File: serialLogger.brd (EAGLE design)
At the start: 63.5 x 50.8 mm, 36 parts, among them J1 Ext Pwr, U1 MCP1702, U2 MCP1700, U3 ATmega328P-AU, U4 74HC4050PW, X1 MICROSD, Y1 16MHz

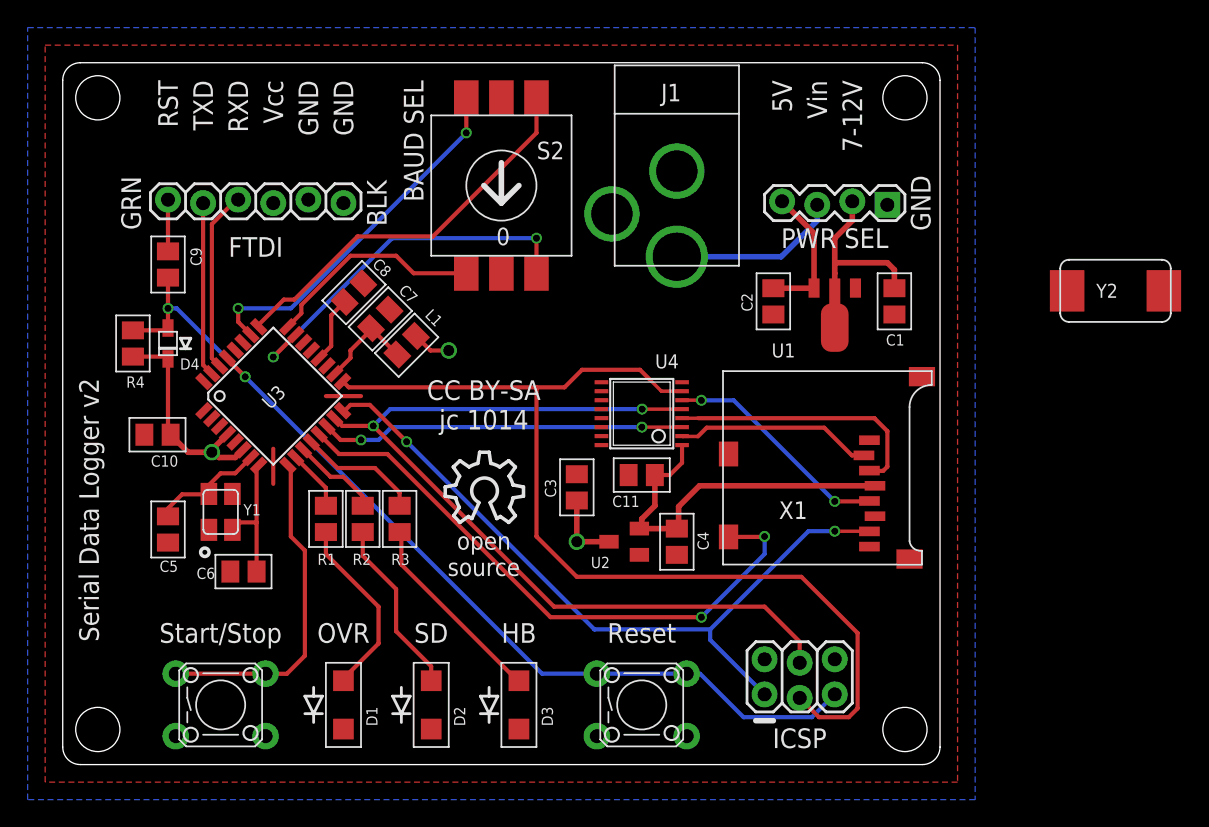
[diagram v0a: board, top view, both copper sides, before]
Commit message: Change to Abracon xtal, refine board, add BOM spreadsheet.
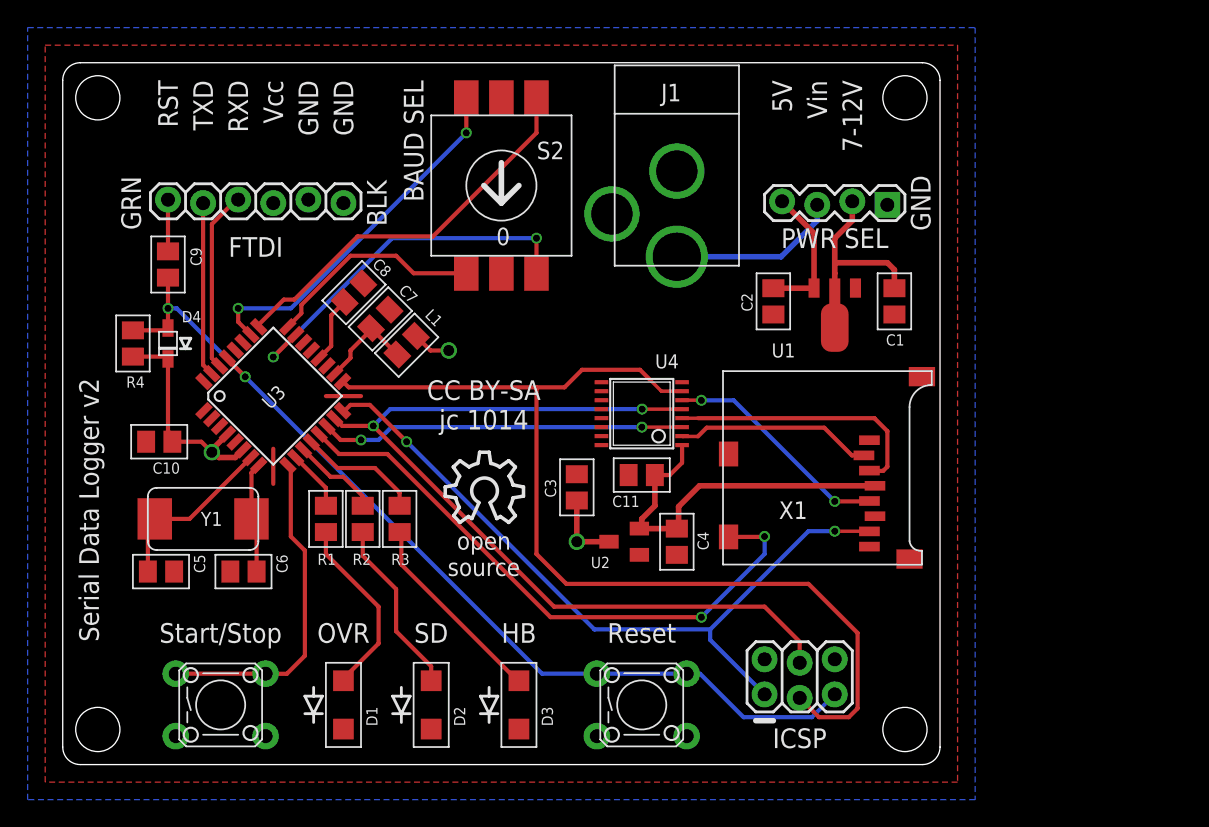
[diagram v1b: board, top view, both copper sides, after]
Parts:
- removed Y2: (no value), _jc:CRYSTAL-ABRACON-ABM2
- C5, C6: value 22pF -> 27pF
- Y1: device _jc:CRYSTAL-EPSON-TSX3225 -> _jc:CRYSTAL-ABRACON-ABM2
- moved C5 3.09 mm to (7.11, 14.0), turned to 0 degrees
- moved Y1 1.37 mm to (10.2, 17.8), turned to 180 degrees
- moved C10 0.52 mm to (6.99, 23.4)
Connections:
- net GND: no longer Y1.2, Y1.4
- net N$18: now also Y1.P$2; no longer Y1.1
- net N$19: now also Y1.P$1; no longer Y1.3
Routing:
- net N$18: track 8.47 -> 12.8 mm
- net N$19: track 9.72 -> 8.06 mm
- net SCK: track 73.3 -> 74.1 mm
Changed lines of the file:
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@@
 <layer number="22" name="bPlace" color="7" fill="1" visible="no" active="yes"/>
 <layer number="23" name="tOrigins" color="15" fill="1" visible="yes" active="yes"/>
-<layer number="24" name="bOrigins" color="15" fill="1" visible="yes" active="yes"/>
+<layer number="24" name="bOrigins" color="15" fill="1" visible="no" active="yes"/>
 <layer number="25" name="tNames" color="7" fill="1" visible="yes" active="yes"/>
 <layer number="26" name="bNames" color="7" fill="1" visible="yes" active="yes"/>
@@
 <layer number="49" name="Reference" color="7" fill="1" visible="yes" active="yes"/>
 <layer number="50" name="dxf" color="7" fill="1" visible="no" active="no"/>
-<layer number="51" name="tDocu" color="7" fill="1" visible="yes" active="yes"/>
+<layer number="51" name="tDocu" color="7" fill="1" visible="no" active="yes"/>
 <layer number="52" name="bDocu" color="7" fill="1" visible="yes" active="yes"/>
 <layer number="53" name="tGND_GNDA" color="7" fill="9" visible="no" active="no"/>
@@
 <attribute name="NAME" x="51.833" y="17.777" size="1.27" layer="25" ratio="16"/>
 </element>
-<element name="C10" library="_jc" package="M0805" value="100nF" x="6.858" y="23.876" smashed="yes" rot="R180">
-<attribute name="NAME" x="8.358" y="22.376003125" size="0.8128" layer="25" ratio="16" rot="R180"/>
-<attribute name="VALUE" x="8.357996875" y="26.376003125" size="0.8128" layer="27" ratio="16" rot="R180"/>
+<element name="C10" library="_jc" package="M0805" value="100nF" x="6.985" y="23.368" smashed="yes" rot="R180">
+<attribute name="NAME" x="8.485" y="21.868003125" size="0.8128" layer="25" ratio="16" rot="R180"/>
+<attribute name="VALUE" x="8.484996875" y="25.868003125" size="0.8128" layer="27" ratio="16" rot="R180"/>
 </element>
 <element name="C11" library="_jc" package="M0805" value="100nF" x="41.91" y="20.955" smashed="yes" rot="R180">
@@
 </element>
 <element name="D4" library="_jc" package="SOD-323F-A" value="1N4148" x="7.62" y="30.48" smashed="yes" rot="R270">
-<attribute name="NAME" x="8.487" y="28.586" size="0.8128" layer="25" font="vector" ratio="16"/>
+<attribute name="NAME" x="8.614" y="32.015" size="0.8128" layer="25" font="vector" ratio="16"/>
 <attribute name="VALUE" x="5.92" y="32.58" size="0.8128" layer="27" font="vector" ratio="16" rot="R270"/>
 </element>
@@
 <attribute name="VALUE" x="21.78910625" y="31.334571875" size="0.8128" layer="27" ratio="16" rot="R45"/>
 </element>
-<element name="C5" library="_jc" package="M0805" value="22pF" x="7.62" y="17.018" smashed="yes" rot="R270">
-<attribute name="NAME" x="7.009" y="13.946" size="0.8128" layer="25" ratio="16"/>
-<attribute name="VALUE" x="5.12" y="18.518" size="0.8128" layer="27" ratio="16" rot="R270"/>
-</element>
-<element name="C6" library="_jc" package="M0805" value="22pF" x="13.081" y="13.97" smashed="yes" rot="R180">
-<attribute name="NAME" x="11.025" y="14.248" size="0.8128" layer="25" ratio="16" rot="R180"/>
+<element name="C5" library="_jc" package="M0805" value="27pF" x="7.112" y="13.97" smashed="yes">
+<attribute name="NAME" x="10.311" y="13.867" size="0.8128" layer="25" ratio="16" rot="R90"/>
+<attribute name="VALUE" x="5.612" y="11.47" size="0.8128" layer="27" ratio="16"/>
+</element>
+<element name="C6" library="_jc" package="M0805" value="27pF" x="13.081" y="13.97" smashed="yes" rot="R180">
+<attribute name="NAME" x="16.28" y="13.867" size="0.8128" layer="25" ratio="16" rot="R90"/>
 <attribute name="VALUE" x="14.581" y="16.47" size="0.8128" layer="27" ratio="16" rot="R180"/>
 </element>
@@
 <attribute name="VALUE" x="24.184890625" y="33.181425" size="0.8128" layer="27" ratio="16" rot="R225"/>
 </element>
-<element name="Y1" library="_jc" package="CRYSTAL-EPSON-TSX3225" value="16MHz" x="11.43" y="18.288" smashed="yes" rot="R270">
-<attribute name="NAME" x="13.081" y="18.034" size="0.8128" layer="25" ratio="16"/>
-<attribute name="VALUE" x="8.89" y="19.558" size="0.8128" layer="27" ratio="16" rot="R270"/>
-</element>
 <element name="U2" library="_jc" package="SOT23" value="MCP1700" x="40.64" y="16.129" smashed="yes" rot="R90">
 <attribute name="NAME" x="38.227" y="14.224" size="0.8128" layer="25" ratio="16"/>
@@
 <element name="LOGO1" library="ohw-logo" package="OSHW_10X200_NOTEXT" value="OSHW_LOGO_10MILX0200-NT" x="27.686" y="17.526"/>
 <element name="LOGO2" library="ohw-logo" package="OSHW_10X200_NOTEXT" value="OSHW_LOGO_10MILX0200-NT" x="32.004" y="37.846" rot="MR0"/>
-<element name="Y2" library="_jc" package="CRYSTAL-ABRACON-ABM2" value="" x="76.2" y="34.29"/>
+<element name="Y1" library="_jc" package="CRYSTAL-ABRACON-ABM2" value="16MHz" x="10.16" y="17.78" rot="R180"/>
 </elements>
 <signals>
@@
 <contactref element="U3" pad="3"/>
 <contactref element="U3" pad="5"/>
-<contactref element="Y1" pad="2"/>
-<contactref element="Y1" pad="4"/>
 <contactref element="C7" pad="2"/>
 <contactref element="C8" pad="2"/>
@@
 <wire x1="5.08" y1="29.53" x2="7.4524" y2="29.53" width="0.3048" layer="1"/>
 <wire x1="7.4524" y1="29.53" x2="7.62" y2="29.3624" width="0.3048" layer="1"/>
-<wire x1="7.808" y1="23.876" x2="9.078" y2="22.606" width="0.4064" layer="1"/>
-<wire x1="9.078" y1="22.606" x2="10.795" y2="22.606" width="0.4064" layer="1"/>
-<wire x1="7.808" y1="23.876" x2="7.62" y2="24.064" width="0.3048" layer="1"/>
-<wire x1="7.62" y1="24.064" x2="7.62" y2="29.3624" width="0.3048" layer="1"/>
+<wire x1="7.62" y1="29.3624" x2="7.62" y2="24.13" width="0.3048" layer="1"/>
+<wire x1="7.62" y1="24.13" x2="7.935" y2="23.815" width="0.3048" layer="1"/>
+<wire x1="7.935" y1="23.815" x2="7.935" y2="23.368" width="0.3048" layer="1"/>
+<wire x1="7.935" y1="23.368" x2="10.033" y2="23.368" width="0.3048" layer="1"/>
+<wire x1="10.033" y1="23.368" x2="10.795" y2="22.606" width="0.3048" layer="1"/>
 </signal>
 <signal name="N$17">
@@
 <wire x1="20.701" y1="27.305" x2="20.280575" y2="27.725425" width="0.3048" layer="1"/>
 <wire x1="20.280575" y1="27.725425" x2="20.255225" y2="27.725425" width="0.3048" layer="1"/>
-<wire x1="34.29" y1="16.51" x2="34.29" y2="27.305" width="0.3048" layer="1"/>
-<wire x1="34.29" y1="16.51" x2="37.211" y2="13.589" width="0.3048" layer="1"/>
-<wire x1="37.211" y1="13.589" x2="53.467" y2="13.589" width="0.3048" layer="1"/>
+<wire x1="34.29" y1="15.24" x2="34.29" y2="27.305" width="0.3048" layer="1"/>
 <wire x1="53.34" y1="4.826" x2="54.737" y2="3.429" width="0.3048" layer="1"/>
 <wire x1="54.737" y1="3.429" x2="56.896" y2="3.429" width="0.3048" layer="1"/>
 <wire x1="56.896" y1="3.429" x2="57.531" y2="4.064" width="0.3048" layer="1"/>
 <wire x1="57.531" y1="4.064" x2="57.531" y2="9.525" width="0.3048" layer="1"/>
-<wire x1="57.531" y1="9.525" x2="53.467" y2="13.589" width="0.3048" layer="1"/>
+<wire x1="36.449" y1="13.081" x2="53.975" y2="13.081" width="0.3048" layer="1"/>
+<wire x1="53.975" y1="13.081" x2="57.531" y2="9.525" width="0.3048" layer="1"/>
+<wire x1="34.29" y1="15.24" x2="36.449" y2="13.081" width="0.3048" layer="1"/>
 </signal>
 <signal name="MISO">
@@
 <contactref element="U3" pad="7"/>
 <contactref element="C5" pad="1"/>
-<contactref element="Y1" pad="1"/>
-<wire x1="13.618884375" y1="22.220459375" x2="12.480425" y2="21.082" width="0.3048" layer="1"/>
-<wire x1="12.480425" y1="21.082" x2="11.43" y2="21.082" width="0.3048" layer="1"/>
-<wire x1="11.43" y1="21.082" x2="10.58" y2="20.232" width="0.3048" layer="1"/>
-<wire x1="10.58" y1="20.232" x2="10.58" y2="19.588" width="0.3048" layer="1"/>
-<wire x1="10.58" y1="19.588" x2="10.55" y2="19.558" width="0.3048" layer="1"/>
-<wire x1="10.55" y1="19.558" x2="8.636" y2="19.558" width="0.3048" layer="1"/>
-<wire x1="8.636" y1="19.558" x2="7.62" y2="18.542" width="0.3048" layer="1"/>
-<wire x1="7.62" y1="18.542" x2="7.62" y2="17.968" width="0.3048" layer="1"/>
+<contactref element="Y1" pad="P$2"/>
+<wire x1="13.618884375" y1="22.220459375" x2="9.178425" y2="17.78" width="0.3048" layer="1"/>
+<wire x1="9.178425" y1="17.78" x2="6.66" y2="17.78" width="0.3048" layer="1"/>
+<wire x1="6.66" y1="17.78" x2="6.162" y2="17.282" width="0.3048" layer="1"/>
+<wire x1="6.162" y1="17.282" x2="6.162" y2="13.97" width="0.3048" layer="1"/>
 </signal>
 <signal name="N$19">
 <contactref element="U3" pad="8"/>
 <contactref element="C6" pad="1"/>
-<contactref element="Y1" pad="3"/>
-<wire x1="14.184571875" y1="21.654771875" x2="14.031" y2="21.5012" width="0.3048" layer="1"/>
-<wire x1="14.031" y1="21.5012" x2="14.031" y2="17.526" width="0.3048" layer="1"/>
-<wire x1="14.031" y1="17.526" x2="14.031" y2="13.97" width="0.3048" layer="1"/>
-<wire x1="12.28" y1="16.988" x2="12.818" y2="17.526" width="0.3048" layer="1"/>
-<wire x1="12.818" y1="17.526" x2="14.031" y2="17.526" width="0.3048" layer="1"/>
+<contactref element="Y1" pad="P$1"/>
+<wire x1="14.184571875" y1="21.654771875" x2="13.66" y2="21.1302" width="0.3048" layer="1"/>
+<wire x1="13.66" y1="21.1302" x2="13.66" y2="17.78" width="0.3048" layer="1"/>
+<wire x1="13.66" y1="17.78" x2="14.031" y2="17.409" width="0.3048" layer="1"/>
+<wire x1="14.031" y1="17.409" x2="14.031" y2="13.97" width="0.3048" layer="1"/>
 </signal>
 <signal name="N$20">

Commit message: Final v2 board
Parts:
- moved C9 1.27 mm to (7.62, 34.9)
- moved J1 1.27 mm to (44.5, 42.0)
- moved JP1 1.27 mm to (20.3, 39.4)
- moved JP3 1.27 mm to (59.7, 39.4)
- moved D4 1.27 mm to (7.62, 29.2)
- moved R4 1.27 mm to (5.08, 29.2)
- moved S2 1.27 mm to (31.8, 40.6)
- moved C2 0.90 mm to (51.3, 32.6)
- moved C1 0.89 mm to (60.2, 32.6)
- moved U1 0.25 mm to (55.9, 32.3)
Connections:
- net ADC3 renamed N$8
- removed net ADC0: S2.4, U3.23
- removed net ADC1: S2.1, U3.24
- removed net ADC2: S2.2, U3.25
- new net N$5: S2.1, U3.23
- new net N$6: S2.2, U3.24
- new net N$7: S2.4, U3.25
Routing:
- net GND: track 5.08 -> 40.8 mm
- net ADC2: track 28.5 -> 0.00 mm
- net ADC0: track 27.4 -> 0.00 mm, vias 2 -> 0
- net N$6: track 0.00 -> 25.8 mm, vias 0 -> 2
- net N$7: track 0.00 -> 24.5 mm
- net N$5: track 0.00 -> 18.5 mm, vias 0 -> 2
- net ADC1: track 15.9 -> 0.00 mm
- net VCC: track 34.6 -> 32.8 mm
- net N$8: track 26.6 -> 28.3 mm
- net RXD: track 13.1 -> 11.8 mm
- net TXD: track 12.6 -> 11.3 mm
- net SCK: track 74.1 -> 75.2 mm
- net N$4: track 16.9 -> 16.2 mm
- net MISO: track 54.3 -> 54.9 mm
- net /RESET: track 69.3 -> 68.8 mm
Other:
- board size 63.5 x 50.8 mm -> 63.5 x 49.5 mm
